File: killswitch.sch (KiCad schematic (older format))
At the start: 3 parts

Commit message: clean up after annotate
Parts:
- gave numbers to parts that had none: 2
- renumbered 10k to 10k1
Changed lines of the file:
@@
 $EndDescr
 $Comp
-L A1120 U?
+L A1120 U9
 U 1 1 595CBD70
 P 6050 4000
-F 0 "U?" H 5850 4300 60  0000 C CNN
+F 0 "U9" H 5850 4300 60  0000 C CNN
 F 1 "A1120" H 5950 3700 60  0000 C CNN
 F 2 "" H 5950 4000 60  0001 C CNN
@@
 $EndComp
 $Comp
-L C C?
+L C C9
 U 1 1 595CBDEE
 P 5250 4200
-F 0 "C?" H 5275 4300 50  0000 L CNN
+F 0 "C9" H 5275 4300 50  0000 L CNN
 F 1 "0.1μ" H 5275 4100 50  0000 L CNN
 F 2 "" H 5288 4050 50  0001 C CNN
@@
 $EndComp
 $Comp
-L GND #PWR?
+L GND #PWR23
 U 1 1 595CBE78
 P 5250 4450
-F 0 "#PWR?" H 5250 4200 50  0001 C CNN
+F 0 "#PWR23" H 5250 4200 50  0001 C CNN
 F 1 "GND" H 5250 4300 50  0000 C CNN
 F 2 "" H 5250 4450 50  0001 C CNN
@@
 	5250 3500 5250 4050
 $Comp
-L GND #PWR?
+L GND #PWR24
 U 1 1 595CBF79
 P 5550 4450
-F 0 "#PWR?" H 5550 4200 50  0001 C CNN
+F 0 "#PWR24" H 5550 4200 50  0001 C CNN
 F 1 "GND" H 5550 4300 50  0000 C CNN
 F 2 "" H 5550 4450 50  0001 C CNN
@@
 	5250 3900 5650 3900
 $Comp
-L R 10k
+L R 10k1
 U 1 1 595CC072
 P 6550 3750
-F 0 "10k" V 6630 3750 50  0000 C CNN
+F 0 "10k1" V 6630 3750 50  0000 C CNN
 F 1 "R" V 6550 3750 50  0000 C CNN
 F 2 "" V 6480 3750 50  0001 C CNN

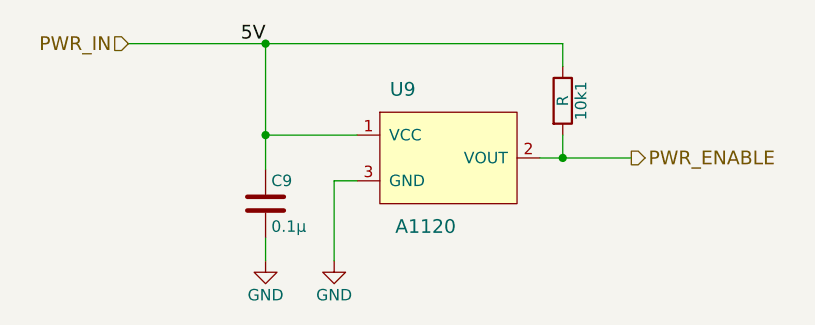
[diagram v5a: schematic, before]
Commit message: fix resistor value
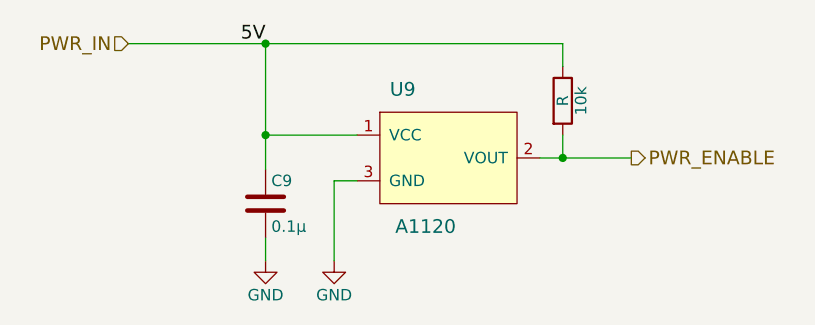
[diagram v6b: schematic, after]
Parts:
- renumbered 10k1 to 10k
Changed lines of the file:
@@
 	5250 3900 5650 3900
 $Comp
-L R 10k1
+L R 10k
 U 1 1 595CC072
 P 6550 3750
-F 0 "10k1" V 6630 3750 50  0000 C CNN
+F 0 "10k" V 6630 3750 50  0000 C CNN
 F 1 "R" V 6550 3750 50  0000 C CNN
 F 2 "" V 6480 3750 50  0001 C CNN

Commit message: fix broken annotation
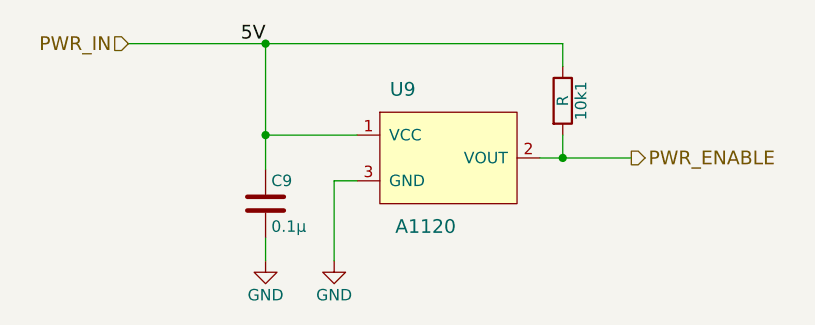
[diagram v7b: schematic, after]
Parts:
- renumbered 10k to 10k1
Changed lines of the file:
@@
 EESchema Schematic File Version 2
+LIBS:pdb-rescue
 LIBS:power
 LIBS:device
@@
 $EndComp
 $Comp
-L GND #PWR23
+L GND #PWR19
 U 1 1 595CBE78
 P 5250 4450
-F 0 "#PWR23" H 5250 4200 50  0001 C CNN
+F 0 "#PWR19" H 5250 4200 50  0001 C CNN
 F 1 "GND" H 5250 4300 50  0000 C CNN
 F 2 "" H 5250 4450 50  0001 C CNN
@@
 	5250 3500 5250 4050
 $Comp
-L GND #PWR24
+L GND #PWR20
 U 1 1 595CBF79
 P 5550 4450
-F 0 "#PWR24" H 5550 4200 50  0001 C CNN
+F 0 "#PWR20" H 5550 4200 50  0001 C CNN
 F 1 "GND" H 5550 4300 50  0000 C CNN
 F 2 "" H 5550 4450 50  0001 C CNN
@@
 	5250 3900 5650 3900
 $Comp
-L R 10k
+L R 10k1
 U 1 1 595CC072
 P 6550 3750
-F 0 "10k" V 6630 3750 50  0000 C CNN
+F 0 "10k1" V 6630 3750 50  0000 C CNN
 F 1 "R" V 6550 3750 50  0000 C CNN
 F 2 "" V 6480 3750 50  0001 C CNN
